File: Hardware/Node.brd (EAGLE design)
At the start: 100 x 80 mm, 30 parts, among them IC1 wiz820io, IC2 MEGA8-P, IC4 LD117AV33, Q1 20MHz

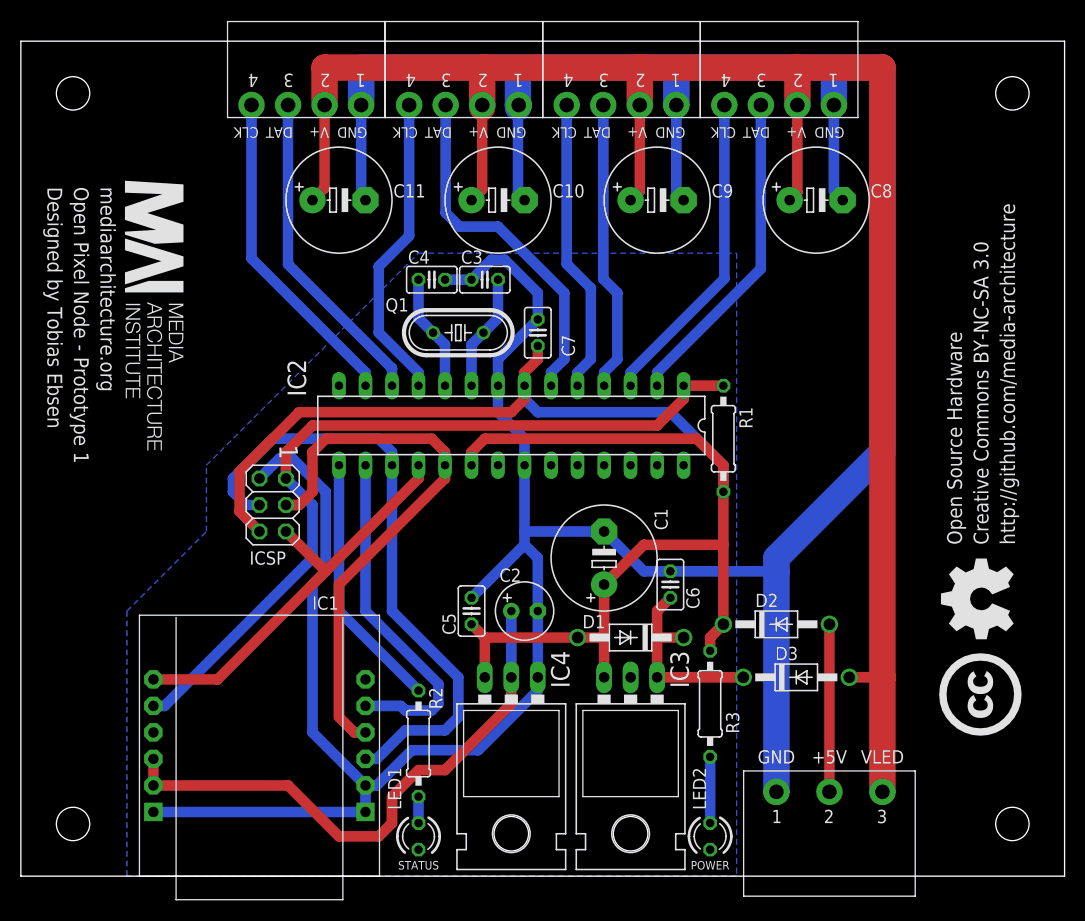
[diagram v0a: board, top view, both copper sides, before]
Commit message: Updated hardware for prototype 2
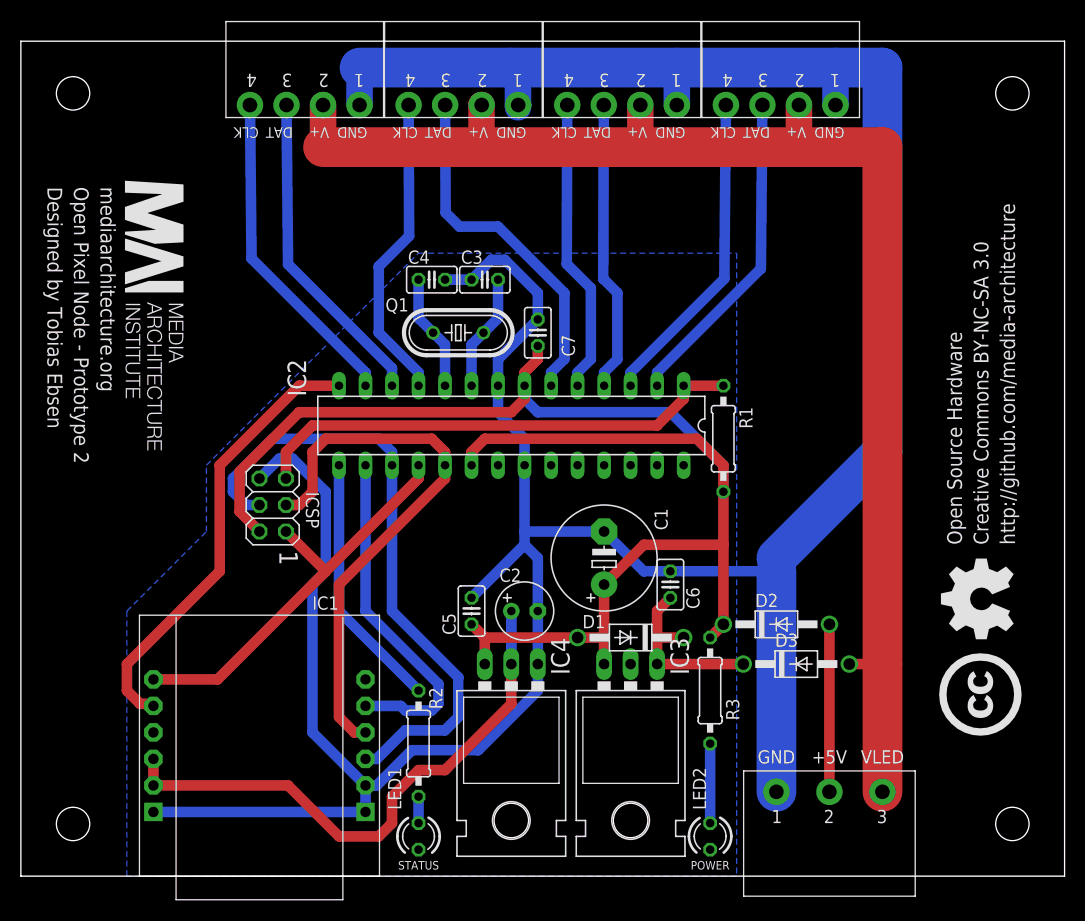
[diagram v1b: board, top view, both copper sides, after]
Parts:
- removed C10, C11, C8, C9: (no value), rcl:E5-10,5
- moved IC3 1.27 mm to (58.4, 16.5)
- moved IC4 1.27 mm to (47.0, 16.5)
- moved D3 1.27 mm to (74.3, 20.3)
- moved R3 1.27 mm to (66.0, 17.8)
- moved U$4 0.15 mm to (27.2, 77.9)
- moved U$1 0.15 mm to (72.8, 77.9)
- moved U$2 0.05 mm to (57.6, 77.9)
- moved U$3 0.05 mm to (42.4, 77.9)
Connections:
- net GND: no longer C10.-, C11.-, C8.-, C9.-
- net N$21: now also IC1.J2.5
- net RESET: no longer IC1.J2.5
- net VCC: no longer C10.+, C11.+, C8.+, C9.+
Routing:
- net VCC: track 178.5 -> 134.7 mm
- net N$21: track 0.00 -> 43.0 mm
- net GND: track 343.3 -> 306.1 mm
- net RESET: track 77.6 -> 47.8 mm
- net +5V: track 152.0 -> 148.2 mm
- net N$9: track 18.9 -> 17.7 mm
- net N$1: track 6.35 -> 7.62 mm
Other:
- board text added: "Open Pixel Node - Prototype 2"
- board text removed: "Open Pixel Node - Prototype 1"
